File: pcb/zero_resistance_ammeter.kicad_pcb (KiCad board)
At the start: 2 copper layers, 40.2 x 44.5 mm, 18 parts, among them J1 Conn_01x03, Q1 2SD636, U1 LM358

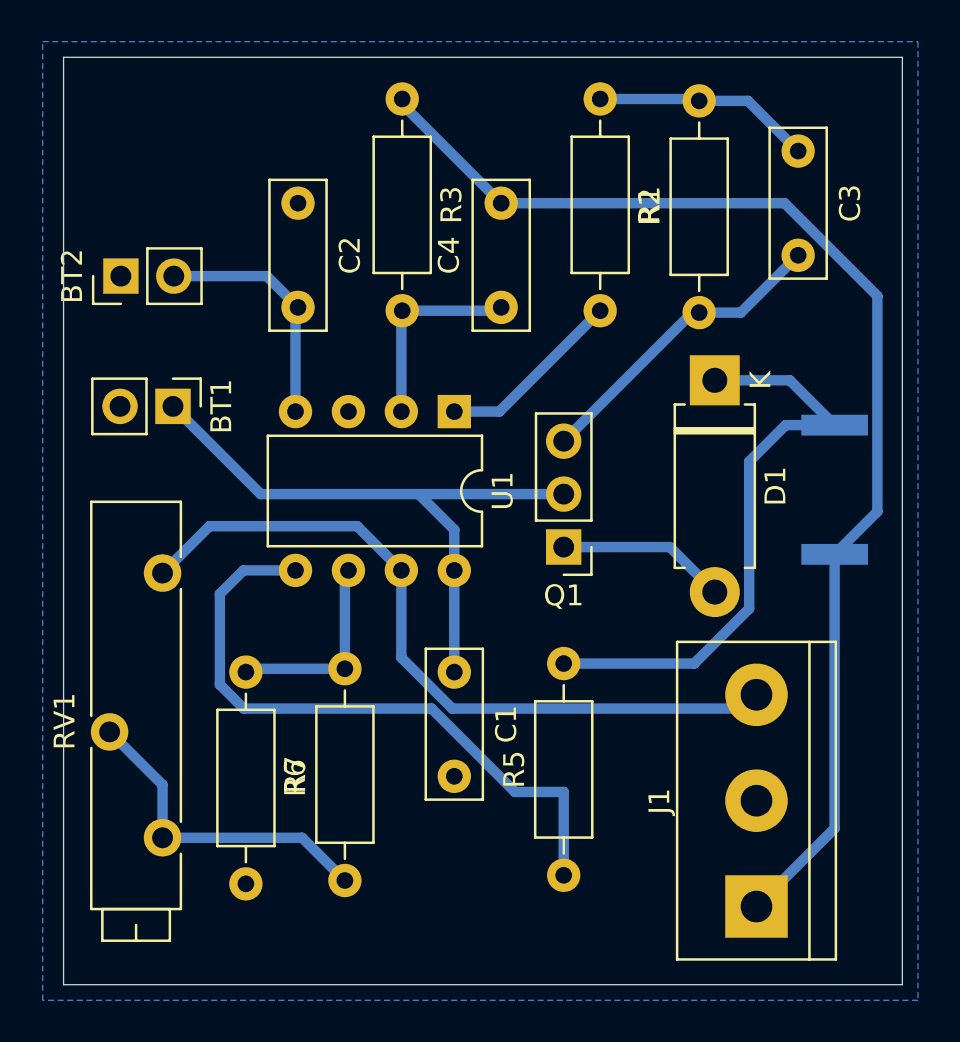
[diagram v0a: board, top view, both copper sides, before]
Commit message: plot gerber and drill
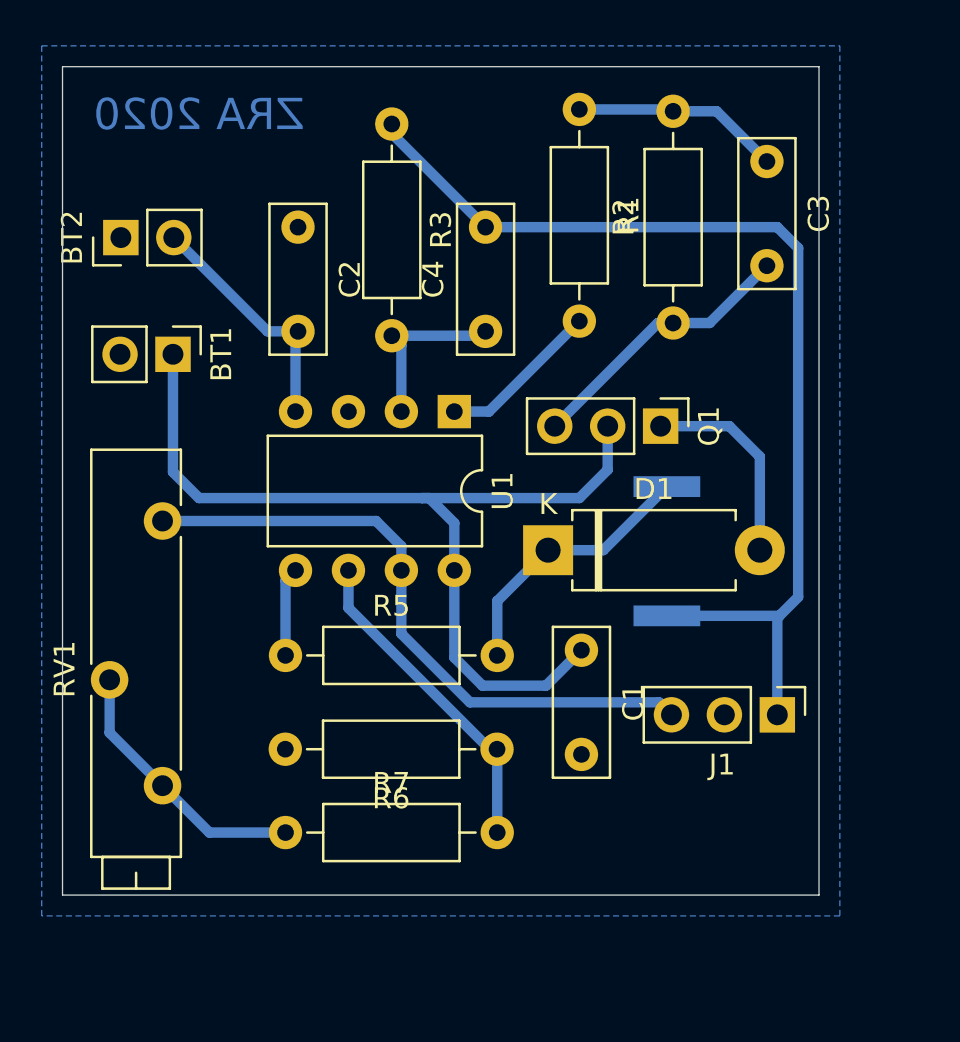
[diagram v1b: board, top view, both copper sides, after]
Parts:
- J1: footprint TerminalBlock:TerminalBlock_bornier-3_P5.08mm -> Connector_PinHeader_2.54mm:PinHeader_1x03_P2.54mm_Vertical
- moved R5 17.0 mm to (125.7, 89.5), turned to 0 degrees
- moved R6 12.6 mm to (135.8, 94.0), turned to 180 degrees
- moved D1 11.4 mm to (138.2, 84.4), turned to 0 degrees
- moved J1 9.25 mm to (149.2, 92.3), turned to 270 degrees
- moved R4 8.57 mm to (143.9, 84.5)
- moved Q1 7.43 mm to (143.7, 78.5), turned to 270 degrees
- moved C1 6.19 mm to (139.8, 89.2)
- moved R7 3.66 mm to (125.7, 98.0), turned to 0 degrees
- moved BT1 2.50 mm to (120.2, 75.0)
- moved RV1 2.50 mm to (119.8, 83.0)
- moved BT2 1.85 mm to (117.8, 69.4)
- moved C3 1.58 mm to (148.8, 65.8)
- moved C4 1.37 mm to (135.2, 73.9)
- moved R2 1.35 mm to (144.2, 73.5)
- moved R3 1.30 mm to (130.8, 64.0)
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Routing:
- net Net-(R5-Pad1): track 31.1 -> 4.28 mm
- net +BATT: track 29.7 -> 45.5 mm
- net Net-(D1-Pad1): track 28.5 -> 13.0 mm
- net Net-(C4-Pad2): track 58.6 -> 50.4 mm
- net Net-(R6-Pad1): track 9.61 -> 15.7 mm
- net Net-(J1-Pad3): track 35.8 -> 30.7 mm
- net Net-(R7-Pad1): track 15.7 -> 13.0 mm
- net Net-(D1-Pad2): track 8.14 -> 9.85 mm
- net Net-(C3-Pad2): track 14.9 -> 13.4 mm
- net Net-(C4-Pad1): track 9.67 -> 8.42 mm
- net Net-(R1-Pad2): track 9.00 -> 7.80 mm
- net Net-(C3-Pad1): track 10.5 -> 10.0 mm
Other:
- board size 40.2 x 44.5 mm -> 36.3 x 39.8 mm
- board text added: "ZRA 2020"
